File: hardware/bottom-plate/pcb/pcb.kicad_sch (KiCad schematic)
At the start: 67 parts, among them SW1 MT-0-102-A101-M200-RS+PJ, SW2 TS4535TP 250GF 009, SW3 TS4535TP 250GF 009

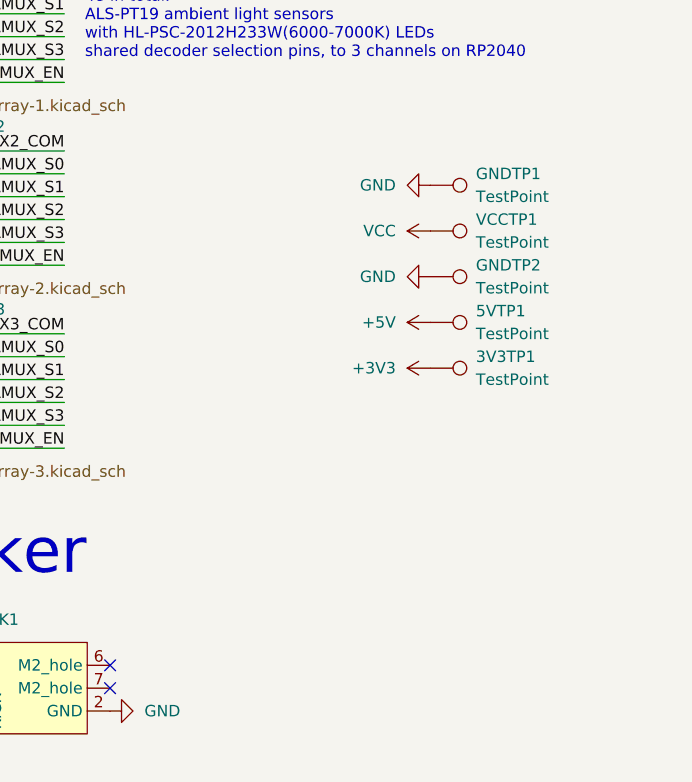
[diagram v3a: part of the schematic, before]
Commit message: labelled bottom middle and top pcbs, added testpoints
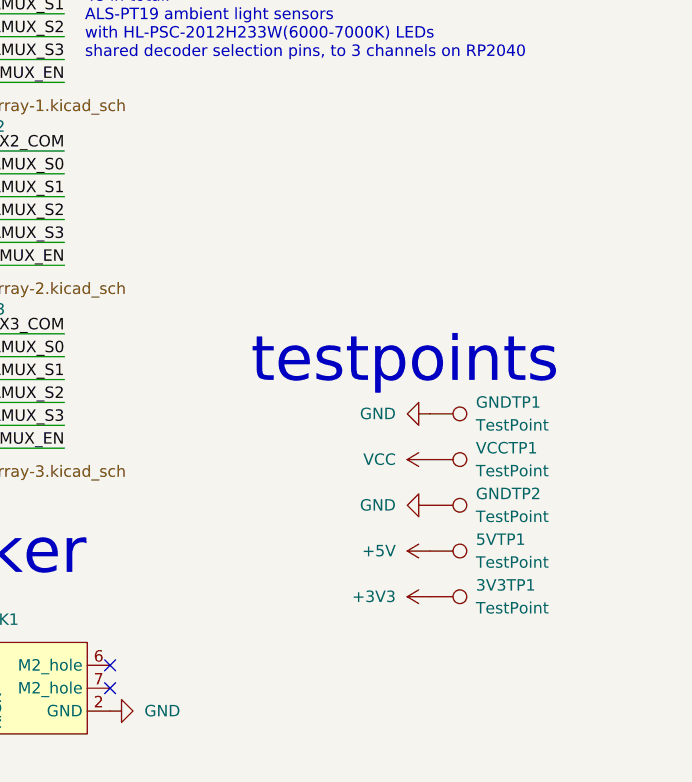
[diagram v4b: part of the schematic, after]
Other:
- note added: "testpoints"
- moved on the sheet: 3V3TP1, 5VTP1, GNDTP1, GNDTP2, VCCTP1
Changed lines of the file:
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@@
 		)
 	)
+	(text "testpoints"
+		(exclude_from_sim no)
+		(at 383.286 90.678 0)
+		(effects
+			(font
+				(size 5 5)
+			)
+		)
+	)
 	(text "mouse sensors"
 		(exclude_from_sim no)
@@
 	(symbol
 		(lib_id "power:GND")
-		(at 386.08 71.12 270)
+		(at 386.08 96.52 270)
 		(unit 1)
 		(exclude_from_sim no)
@@
 		(fields_autoplaced yes)
 		(property "Reference" "#PWR0281"
-			(at 379.73 71.12 0)
+			(at 379.73 96.52 0)
 			(effects
 				(font
@@
 		)
 		(property "Value" "GND"
-			(at 382.27 71.1199 90)
+			(at 382.27 96.5199 90)
 			(effects
 				(font
@@
 		)
 		(property "Footprint" ""
-			(at 386.08 71.12 0)
+			(at 386.08 96.52 0)
 			(effects
 				(font
@@
 		)
 		(property "Datasheet" ""
-			(at 386.08 71.12 0)
+			(at 386.08 96.52 0)
 			(effects
 				(font
@@
 		)
 		(property "Description" "Power symbol creates a global label with name \"GND\" , ground"
-			(at 386.08 71.12 0)
+			(at 386.08 96.52 0)
 			(effects
 				(font
@@
 	(symbol
 		(lib_id "power:+5V")
-		(at 386.08 86.36 90)
+		(at 386.08 111.76 90)
 		(mirror x)
 		(unit 1)
@@
 		(fields_autoplaced yes)
 		(property "Reference" "#PWR0283"
-			(at 389.89 86.36 0)
+			(at 389.89 111.76 0)
 			(effects
 				(font
@@
 		)
 		(property "Value" "+5V"
-			(at 382.27 86.3599 90)
+			(at 382.27 111.7599 90)
 			(effects
 				(font
@@
 		)
 		(property "Footprint" ""
-			(at 386.08 86.36 0)
+			(at 386.08 111.76 0)
 			(effects
 				(font
@@
 		)
 		(property "Datasheet" ""
-			(at 386.08 86.36 0)
+			(at 386.08 111.76 0)
 			(effects
 				(font
@@
 		)
 		(property "Description" "Power symbol creates a global label with name \"+5V\""
-			(at 386.08 86.36 0)
+			(at 386.08 111.76 0)
 			(effects
 				(font
@@
 	(symbol
 		(lib_id "Connector:TestPoint")
-		(at 386.08 71.12 270)
+		(at 386.08 96.52 270)
 		(unit 1)
 		(exclude_from_sim no)
@@
 		(fields_autoplaced yes)
 		(property "Reference" "GNDTP1"
-			(at 391.16 69.8499 90)
+			(at 391.16 95.2499 90)
 			(effects
 				(font
@@
 		)
 		(property "Value" "TestPoint"
-			(at 391.16 72.3899 90)
+			(at 391.16 97.7899 90)
 			(effects
 				(font
@@
 		)
 		(property "Footprint" "TestPoint:TestPoint_THTPad_D1.0mm_Drill0.5mm"
-			(at 386.08 76.2 0)
+			(at 386.08 101.6 0)
 			(effects
 				(font
@@
 		)
 		(property "Datasheet" "~"
-			(at 386.08 76.2 0)
+			(at 386.08 101.6 0)
 			(effects
 				(font
@@
 		)
 		(property "Description" "test point"
-			(at 386.08 71.12 0)
+			(at 386.08 96.52 0)
 			(effects
 				(font
@@
 	(symbol
 		(lib_id "Connector:TestPoint")
-		(at 386.08 81.28 270)
+		(at 386.08 106.68 270)
 		(unit 1)
 		(exclude_from_sim no)
@@
 		(fields_autoplaced yes)
 		(property "Reference" "GNDTP2"
-			(at 391.16 80.0099 90)
+			(at 391.16 105.4099 90)
 			(effects
 				(font
@@
 		)
 		(property "Value" "TestPoint"
-			(at 391.16 82.5499 90)
+			(at 391.16 107.9499 90)
 			(effects
 				(font
@@
 		)
 		(property "Footprint" "TestPoint:TestPoint_THTPad_D1.0mm_Drill0.5mm"
-			(at 386.08 86.36 0)
+			(at 386.08 111.76 0)
 			(effects
 				(font
@@
 		)
 		(property "Datasheet" "~"
-			(at 386.08 86.36 0)
+			(at 386.08 111.76 0)
 			(effects
 				(font
@@
 		)
 		(property "Description" "test point"
-			(at 386.08 81.28 0)
+			(at 386.08 106.68 0)
 			(effects
 				(font
@@
 	(symbol
 		(lib_id "Connector:TestPoint")
-		(at 386.08 76.2 270)
+		(at 386.08 101.6 270)
 		(unit 1)
 		(exclude_from_sim no)
@@
 		(fields_autoplaced yes)
 		(property "Reference" "VCCTP1"
-			(at 391.16 74.9299 90)
+			(at 391.16 100.3299 90)
 			(effects
 				(font
@@
 		)
 		(property "Value" "TestPoint"
-			(at 391.16 77.4699 90)
+			(at 391.16 102.8699 90)
 			(effects
 				(font
@@
 		)
 		(property "Footprint" "TestPoint:TestPoint_THTPad_D1.0mm_Drill0.5mm"
-			(at 386.08 81.28 0)
+			(at 386.08 106.68 0)
 			(effects
 				(font
@@
 		)
 		(property "Datasheet" "~"
-			(at 386.08 81.28 0)
+			(at 386.08 106.68 0)
 			(effects
 				(font
@@
 		)
 		(property "Description" "test point"
-			(at 386.08 76.2 0)
+			(at 386.08 101.6 0)
 			(effects
 				(font
@@
 	(symbol
 		(lib_id "power:GND")
-		(at 386.08 81.28 270)
+		(at 386.08 106.68 270)
 		(unit 1)
 		(exclude_from_sim no)
@@
 		(fields_autoplaced yes)
 		(property "Reference" "#PWR0285"
-			(at 379.73 81.28 0)
+			(at 379.73 106.68 0)
 			(effects
 				(font
@@
 		)
 		(property "Value" "GND"
-			(at 382.27 81.2799 90)
+			(at 382.27 106.6799 90)
 			(effects
 				(font
@@
 		)
 		(property "Footprint" ""
-			(at 386.08 81.28 0)
+			(at 386.08 106.68 0)
 			(effects
 				(font
@@
 		)
 		(property "Datasheet" ""
-			(at 386.08 81.28 0)
+			(at 386.08 106.68 0)
 			(effects
 				(font
@@
 		)
 		(property "Description" "Power symbol creates a global label with name \"GND\" , ground"
-			(at 386.08 81.28 0)
+			(at 386.08 106.68 0)
 			(effects
 				(font
@@
 	(symbol
 		(lib_id "power:+3V3")
-		(at 386.08 91.44 90)
+		(at 386.08 116.84 90)
 		(unit 1)
 		(exclude_from_sim no)
@@
 		(fields_autoplaced yes)
 		(property "Reference" "#PWR0284"
-			(at 389.89 91.44 0)
+			(at 389.89 116.84 0)
 			(effects
 				(font
@@
 		)
 		(property "Value" "+3V3"
-			(at 382.27 91.4399 90)
+			(at 382.27 116.8399 90)
 			(effects
 				(font
@@
 		)
 		(property "Footprint" ""
-			(at 386.08 91.44 0)
+			(at 386.08 116.84 0)
 			(effects
 				(font
@@
 		)
 		(property "Datasheet" ""
-			(at 386.08 91.44 0)
+			(at 386.08 116.84 0)
 			(effects
 				(font
@@
 		)
 		(property "Description" "Power symbol creates a global label with name \"+3V3\""
-			(at 386.08 91.44 0)
+			(at 386.08 116.84 0)
 			(effects
 				(font
@@
 	(symbol
 		(lib_id "Connector:TestPoint")
-		(at 386.08 91.44 270)
+		(at 386.08 116.84 270)
 		(unit 1)
 		(exclude_from_sim no)
@@
 		(fields_autoplaced yes)
 		(property "Reference" "3V3TP1"
-			(at 391.16 90.1699 90)
+			(at 391.16 115.5699 90)
 			(effects
 				(font
@@
 		)
 		(property "Value" "TestPoint"
-			(at 391.16 92.7099 90)
+			(at 391.16 118.1099 90)
 			(effects
 				(font
@@
 		)
 		(property "Footprint" "TestPoint:TestPoint_THTPad_D1.0mm_Drill0.5mm"
-			(at 386.08 96.52 0)
+			(at 386.08 121.92 0)
 			(effects
 				(font
@@
 		)
 		(property "Datasheet" "~"
-			(at 386.08 96.52 0)
+			(at 386.08 121.92 0)
 			(effects
 				(font
@@
 		)
 		(property "Description" "test point"
-			(at 386.08 91.44 0)
+			(at 386.08 116.84 0)
 			(effects
 				(font
@@
 	(symbol
 		(lib_id "Connector:TestPoint")
-		(at 386.08 86.36 270)
+		(at 386.08 111.76 270)
 		(unit 1)
 		(exclude_from_sim no)
@@
 		(fields_autoplaced yes)
 		(property "Reference" "5VTP1"
-			(at 391.16 85.0899 90)
+			(at 391.16 110.4899 90)
 			(effects
 				(font
@@
 		)
 		(property "Value" "TestPoint"
-			(at 391.16 87.6299 90)
+			(at 391.16 113.0299 90)
 			(effects
 				(font
@@
 		)
 		(property "Footprint" "TestPoint:TestPoint_THTPad_D1.0mm_Drill0.5mm"
-			(at 386.08 91.44 0)
+			(at 386.08 116.84 0)
 			(effects
 				(font
@@
 		)
 		(property "Datasheet" "~"
-			(at 386.08 91.44 0)
+			(at 386.08 116.84 0)
 			(effects
 				(font
@@
 		)
 		(property "Description" "test point"
-			(at 386.08 86.36 0)
+			(at 386.08 111.76 0)
 			(effects
 				(font
@@
 	(symbol
 		(lib_id "power:+12V")
-		(at 386.08 76.2 90)
+		(at 386.08 101.6 90)
 		(unit 1)
 		(exclude_from_sim no)
@@
 		(fields_autoplaced yes)
 		(property "Reference" "#PWR0282"
-			(at 389.89 76.2 0)
+			(at 389.89 101.6 0)
 			(effects
 				(font
@@
 		)
 		(property "Value" "VCC"
-			(at 382.27 76.1999 90)
+			(at 382.27 101.5999 90)
 			(effects
 				(font
@@
 		)
 		(property "Footprint" ""
-			(at 386.08 76.2 0)
+			(at 386.08 101.6 0)
 			(effects
 				(font
@@
 		)
 		(property "Datasheet" ""
-			(at 386.08 76.2 0)
+			(at 386.08 101.6 0)
 			(effects
 				(font
@@
 		)
 		(property "Description" "Power symbol creates a global label with name \"+12V\""
-			(at 386.08 76.2 0)
+			(at 386.08 101.6 0)
 			(effects
 				(font

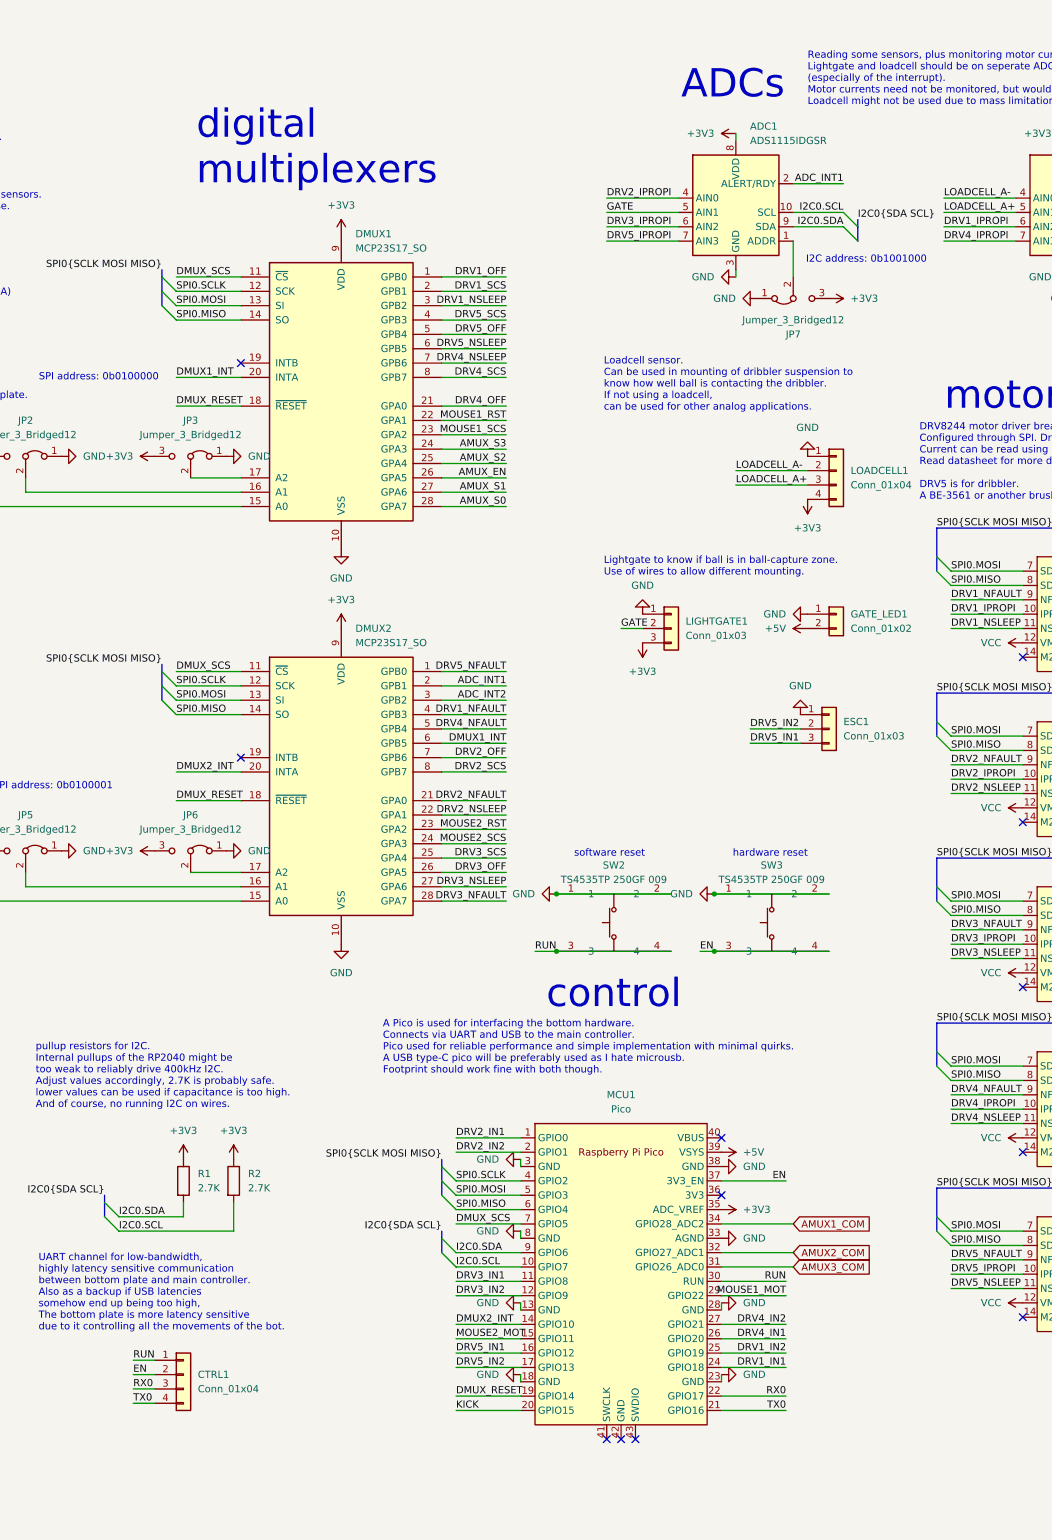
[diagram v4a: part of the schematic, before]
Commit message: added capacitors for motor drivers
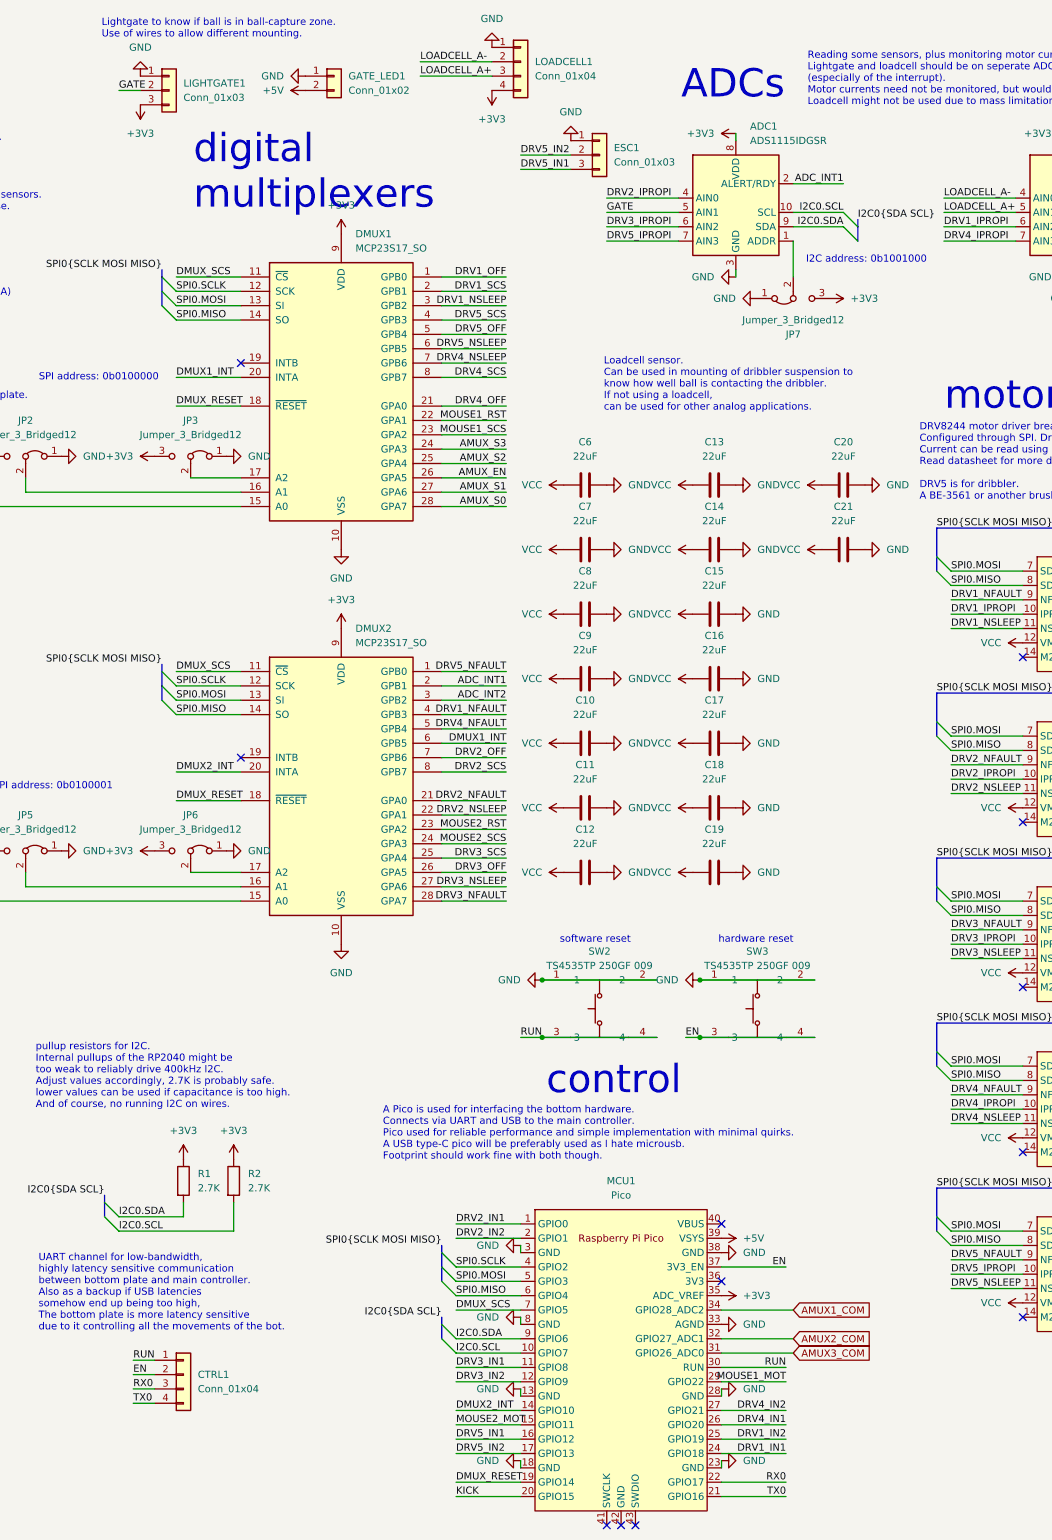
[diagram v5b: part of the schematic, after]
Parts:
- added C10, C11, C12, C13, C14, C15, C16, C17, C18, C19, C20, C21, C6, C7, C8, C9: 22uF, PCM_Capacitor_SMD_AKL:C_0805_2012Metric_Pad1.15x1.40mm_HandSolder, symbol Device:C
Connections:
- net GND: now also C10.2, C11.2, C12.2, C13.2, C14.2, C15.2, C16.2, C17.2, C18.2, C19.2, C20.2, C21.2, C6.2, C7.2, C8.2, C9.2
- net VCC: now also C10.1, C11.1, C12.1, C13.1, C14.1, C15.1, C16.1, C17.1, C18.1, C19.1, C20.1, C21.1, C6.1, C7.1, C8.1, C9.1
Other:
- moved on the sheet: ESC1, GATE_LED1, LIGHTGATE1, LOADCELL1, MCU1, SW2, SW3

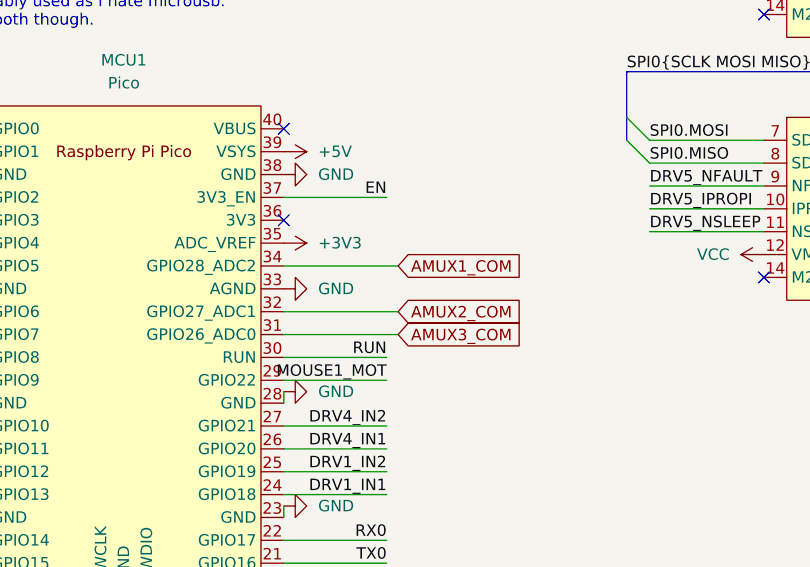
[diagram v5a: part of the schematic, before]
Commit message: removed global labels from bottom plate schematic (forgot to remove it)
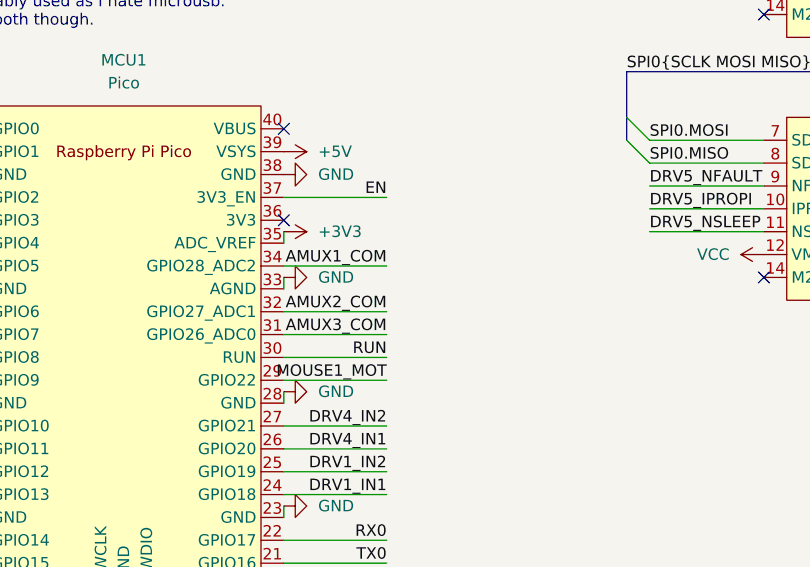
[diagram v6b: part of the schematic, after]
